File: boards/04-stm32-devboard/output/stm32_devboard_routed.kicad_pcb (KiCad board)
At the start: 2 copper layers, 60 x 40 mm, 17 parts, among them J1 SWD, U1 AMS1117-3.3, U2 STM32F103C8T6, Y1 8MHz

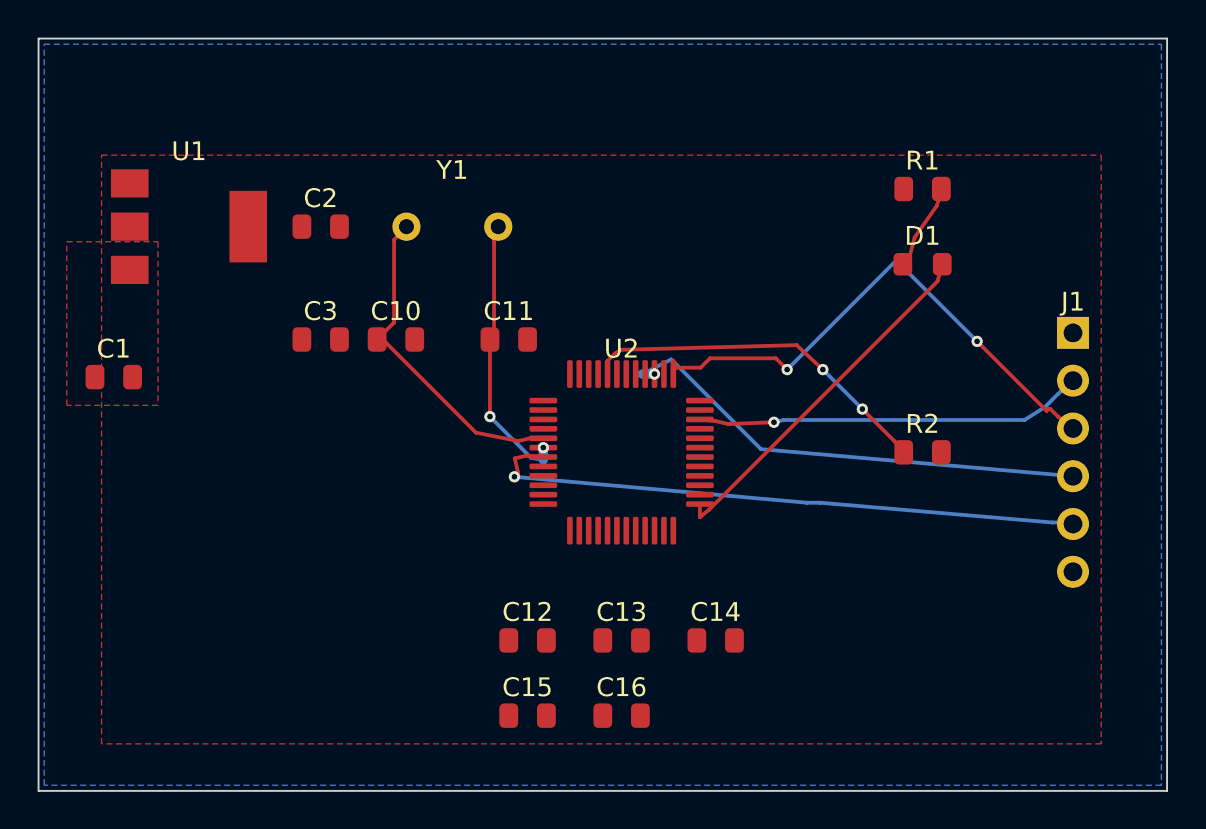
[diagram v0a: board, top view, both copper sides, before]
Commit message: feat(router,board-04): --micro-via stitch + --strict-in-pad-clearance opt-in (closes #3033) (#3038)
* feat(cli): expose --micro-via on outer kct stitch (forward from parser to subprocess)

The stitch_cmd module already supported --micro-via / --micro-via-size /
--micro-via-drill (PR #2786) but only at its own argparse layer.  The
outer ``kct stitch`` wrapper in cli/parser.py didn't register the
flags, so ``kct stitch board.kicad_pcb --net GND --micro-via`` returned
``error: unrecognized arguments: --micro-via``.

Fix: register the three micro-via args on ``stitch_parser`` (matching
the inner parser's dest names with the ``stitch_`` prefix) and forward
them through ``_run_stitch_command`` to the subprocess argv.  Behaviour
is unchanged when the flags are omitted; the inner defaults (0.3mm pad
/ 0.15mm drill) are forwarded as-is.

This unblocks board-04's LQFP-48 corner GND stitch (issue #3033): the
U2.23 corner pad now stitches cleanly with a micro-via after the
standard 0.6mm via collides with neighbour escape traces.  U2.8 is
still blocked (separate OSC_OUT-via track on B.Cu).

Co-Authored-By: Claude Opus 4.7 (1M context) <noreply@anthropic.com>

* fix(board-04): use --micro-via for GND stitch, refresh manufacturing bundle (closes #3033)

Adopts the new ``kct stitch --micro-via`` flag (added in the same PR's
feat(cli) commit) to recover board-04's U2.23 LQFP-48 corner GND pad
that the default 0.6mm via cannot fit between neighbour escape traces.
Stitcher reports go from 2 skipped GND pads -> 1 (U2.8 only, blocked
by an OSC_OUT B.Cu trace from the in-pad rescue -- separate cluster).

The regenerated manufacturing bundle restores manifest mtime > routed
PCB mtime so ``kct fleet status`` no longer reports the artifacts as
stale.

End-state on this PR vs. the pre-PR committed baseline:

| metric                          | pre-PR | post-PR | AC target |
|---------------------------------|--------|---------|-----------|
| nets complete / total           | 11/12  | 11/12 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
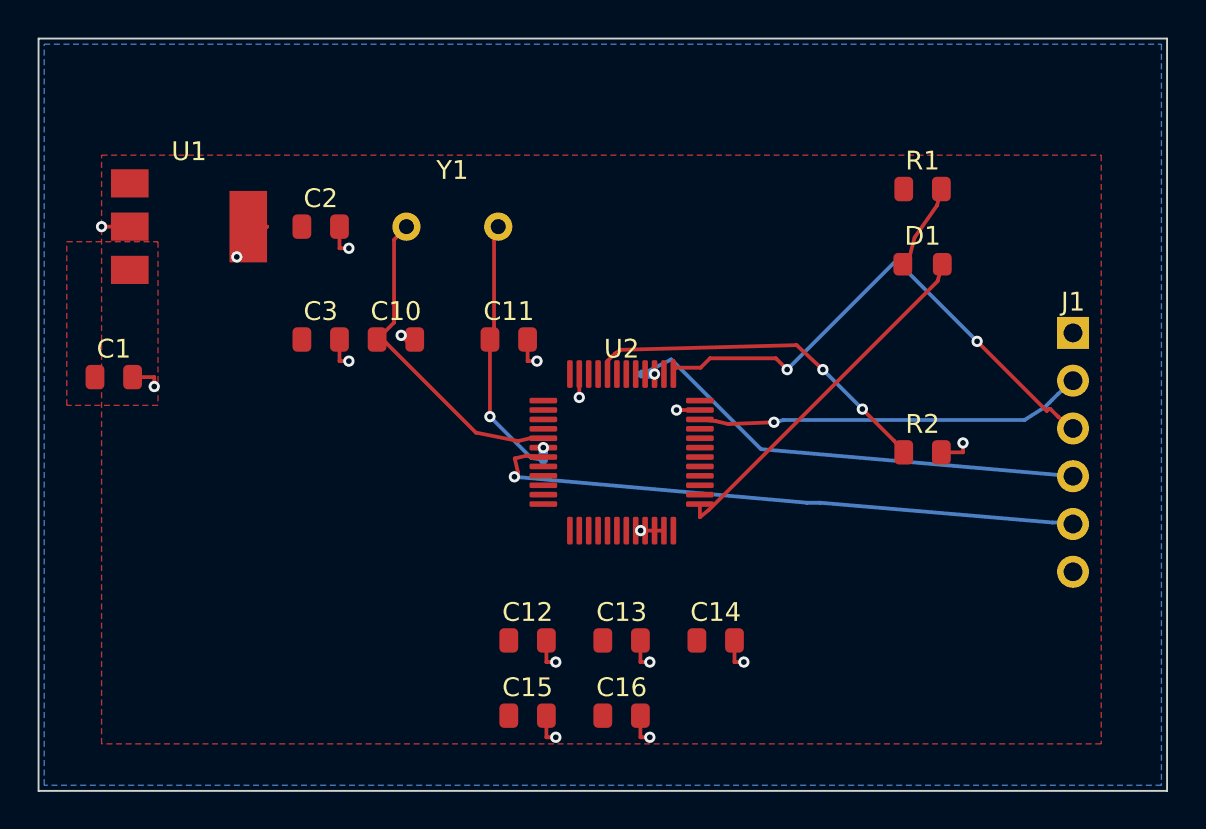
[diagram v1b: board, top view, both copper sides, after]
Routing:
- net GND: track 0.00 -> 26.5 mm, vias 0 -> 16

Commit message: feat(router): micro-via in-pad rescue for non-GND fine-pitch escape (closes #3118) (#3128)
When the standard manufacturer-floor via (0.6 mm OD / 0.3 mm drill on
jlcpcb-tier1) clips a foreign-net neighbour on a fine-pitch
QFP/SSOP/LQFP pad, the in-pad escape now retries with a micro-via
(default 0.3 mm OD / 0.15 mm drill) when the new
``--micro-via-in-pad-fallback`` flag is set.  The emitted via carries
``is_micro=True`` so it serialises as ``(via micro ...)`` and the
dimensions DRC exempts it from the standard min-via floors.

On board-04 (STM32 devboard, LQFP-48 0.5 mm-pitch), this resolves the
OSC_OUT cluster outright: pre-fix 4 errors (2 ``clearance_segment_via``
+ 2 ``clearance_pad_via`` at U2.5/U2.7) drop to 0.  The drc tolerance
floor for ``boards/04-stm32-devboard/output/stm32_devboard_routed.kicad_pcb``
is decremented 4 -> 1 (the remaining 1 is the historically-unstable
SWDIO/BOOT0 site at PCB (143.8, 119.7), separate cluster).

Implementation:
* ``EscapeRouter.__init__`` reads
  ``KICAD_TOOLS_MICRO_VIA_IN_PAD_FALLBACK`` /
  ``KICAD_TOOLS_MICRO_VIA_SIZE`` /
  ``KICAD_TOOLS_MICRO_VIA_DRILL`` env vars so the lazily-constructed
  router instances inherit the opt-in across all 3 construction sites
  (orchestrator + core) without new positional args.
* ``_try_in_pad_escape`` runs the micro-via retry inside the existing
  ``_via_clears_other_pads`` rejection branch (no new dispatcher args),
  re-checks geometry and clearance, and only commits the micro-via
  when both gates pass.
* CLI flags ``--micro-via-in-pad-fallback`` / ``--micro-via-size`` /
  ``--micro-via-drill`` added on both the outer ``kct route`` parser
  (forwarding) and the inner ``route_cmd.main`` (env-stamping).
* ``boards/04-stm32-devboard/generate_design.py`` now passes
  ``--micro-via-in-pad-fallback`` on its ``kct route`` invocation.

Micro-via preservation through the route pipeline (companion fixes to
#3124/#3126):
* ``EscapeRouter._apply_edge_clearance`` -- the edge-clamp rebuilt the
  Via w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
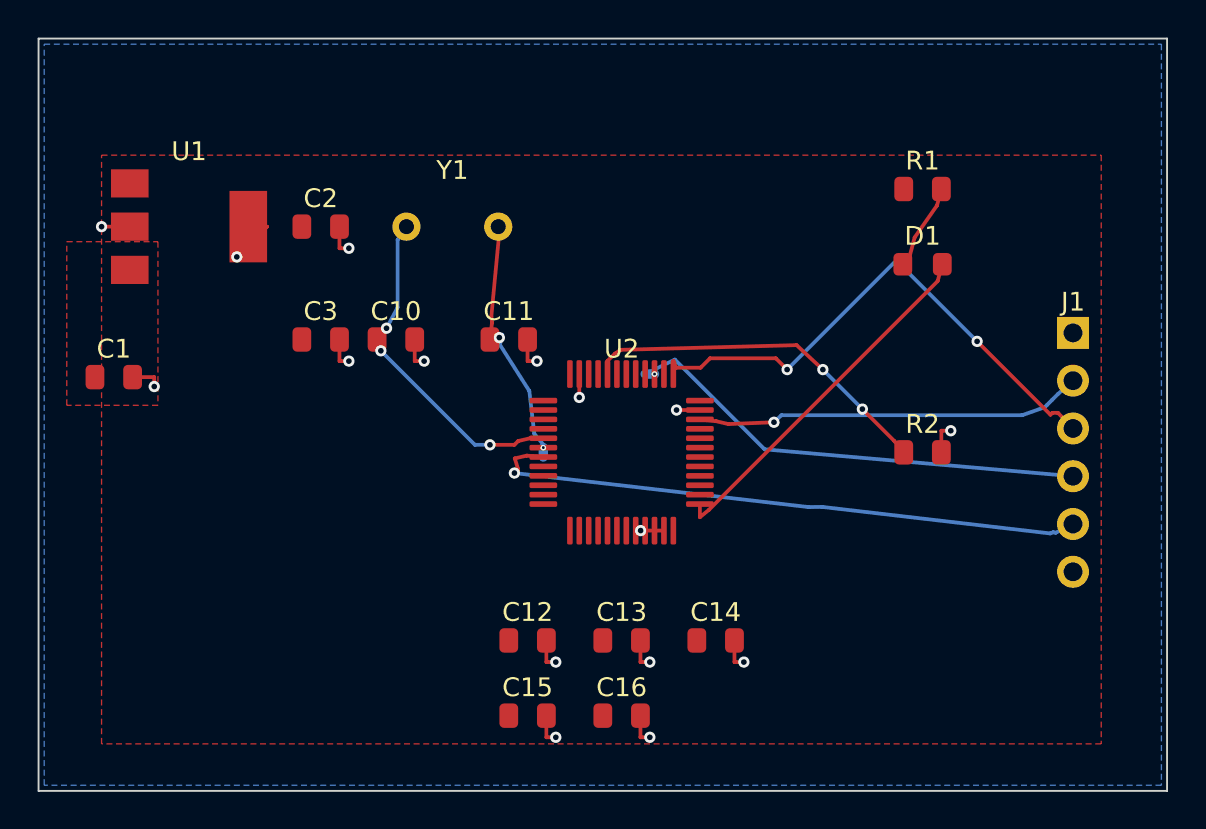
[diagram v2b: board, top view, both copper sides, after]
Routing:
- net OSC_IN: track 17.5 -> 17.9 mm, vias 0 -> 3

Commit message: fix(board-04): document NRST clearance regression, refresh routed PCB (closes #3266)
The post-#3128 clearance-tightening cluster (#3225/#3227 foreign-pad
clearance, #3232/#3248 Chebyshev -> Euclidean disc kernel, #3250
sub-cell pad-metal margin) correctly closes a ~0.125mm pad-clearance
corridor between U2.7 (NRST) and U2.8 (GND) that the prior committed
routed PCB exploited.  Re-running the production recipe now lands 8/9
signal nets routed (NRST stranded at J1.5).

Diagnosis:
- The prior committed PCB at PR #3128 had NRST F.Cu running through
  the U2.7/U2.8 channel at ~0.125mm pad clearance -- BELOW the
  jlcpcb-tier1 0.127mm minimum.  Verified by checking out 62918dfb and
  re-running the recipe: the recipe at that commit also produces 8/9,
  so the committed routed PCB at #3128 was hand-preserved from an
  earlier router state, not regenerated.
- The current router correctly refuses to thread NRST through the
  marginal corridor.  No single PR in the post-#3128 router cluster is
  the sole regression source; the cumulative tightening is correct
  behaviour.
- The refreshed PCB has 0 blocking DRC errors (vs 1
  clearance_segment_via on the prior committed artifact); 2 advisory
  connectivity findings (NRST + GND U2.8/U2.35 stitch skips) are
  excluded from the CI gate per DRCChecker.ADVISORY_RULE_IDS (#3074).

Functional implication: SWD hardware reset is unavailable
(software-mediated reset through the SWD probe is unaffected).
Recovery options documented in the tolerance YAML; underlying cluster
rides with #2834 manufacturing-ready.

Changes:
- Refresh boards/04-stm32-devboard/output/stm32_devboard_routed.kicad_pcb
  (and the input schematic/PCB which only diff by random UUIDs) via
  the production recipe.
- Drop the CI gate floor for board 04: 1 -> 0 (the refreshed PCB has
  no blocking errors; the prior 1-error SWDIO/BOOT0 clearance_segment_via
  is gone).
- Document the regression mechanism and recovery options in both
  generate_design.py::route_pcb and th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
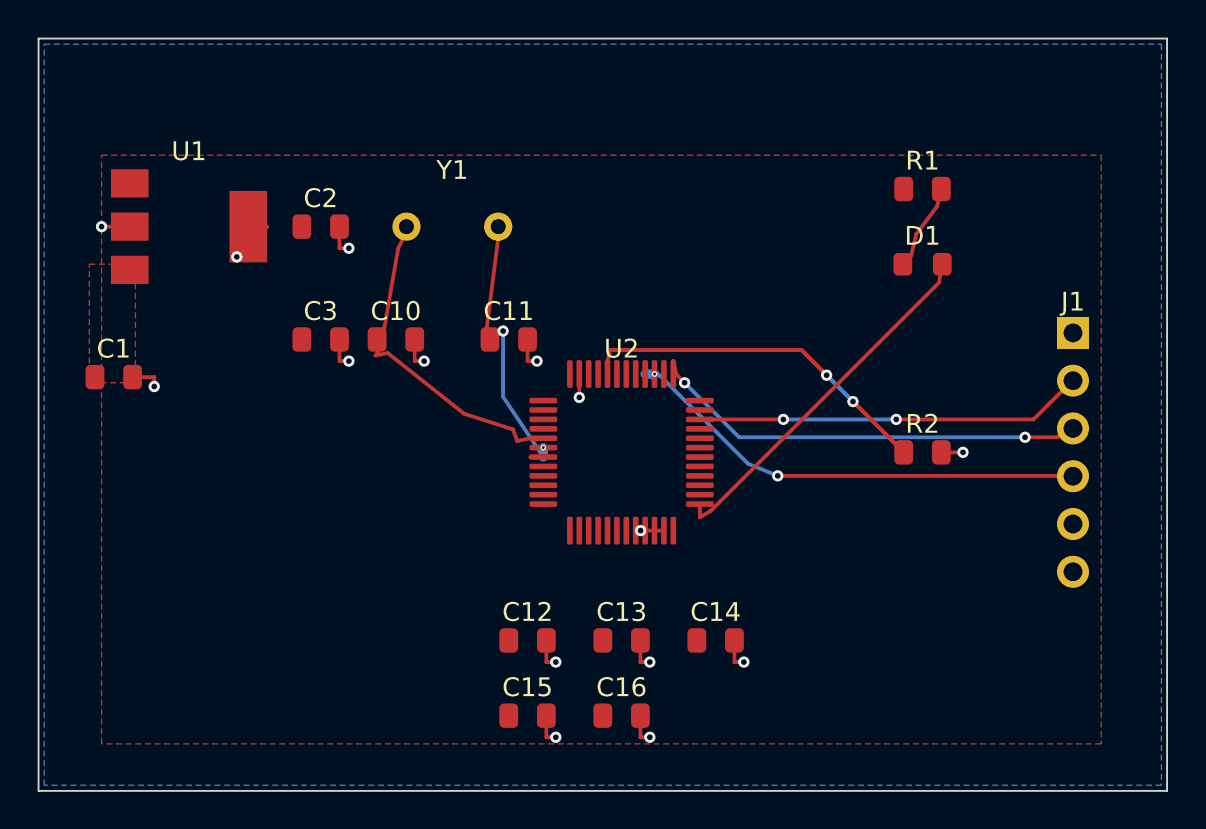
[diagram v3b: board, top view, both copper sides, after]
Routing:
- net NRST: track 32.4 -> 0.70 mm, vias 1 -> 0
- net SWCLK: track 28.8 -> 24.0 mm
- net GND: track 26.6 -> 24.9 mm, vias 16 -> 15
- net OSC_OUT: track 14.4 -> 15.0 mm
- net SWO: track 25.5 -> 25.3 mm, vias 1 -> 2
- net OSC_IN: track 17.9 -> 17.8 mm, vias 3 -> 0
- net SWDIO: track 20.6 -> 20.7 mm, vias 1 -> 2

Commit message: fix(router): seg-seg violations in negotiated quality tuple + demote-to-partial (refs #3411, closes #3433)
Closes #3433

Four coordinated fixes for the env-sensitive board-04 SWCLK/SWO
-0.200mm trace-overlap commits:

1. find_nets_with_segment_segment_violations completes the clearance
   matrix in the IterationMetrics lex tuple at all metric sites
   (core.py init/post/top-of-iter/final + two_phase.py equivalents),
   plus mid-iteration rip-up feed of both nets of each overlapping pair.
2. Demote-to-partial safety net: physically-overlapping copper
   (copper_overlap_only pairs) is stripped via greedy vertex cover
   rather than committed -- unrouted is advisory, overlap is a hard
   gate failure.
3. GridCollisionChecker.ignore_overflow scoped to genuinely overused
   cells (usage_count > 1): the #2303 blanket skip let the staircase
   compressor straighten SWO across SWCLK whenever ANY residual
   overflow existed (env-sensitive: rtree-equipped machines used the
   vector checker and never saw it).
4. Rect-aware stitch straight-trace pad check (find_all_pad_bboxes):
   the U2.8->U2.9 pad crossing was the lone remaining blocking error
   in the refreshed artifact.

Board-04 artifact refreshed at the production recipe: 9/9 routed
(NRST recovered per #3434), 0 blocking errors, floor stays 0.

Co-Authored-By: Claude Opus 4.7 <noreply@anthropic.com>
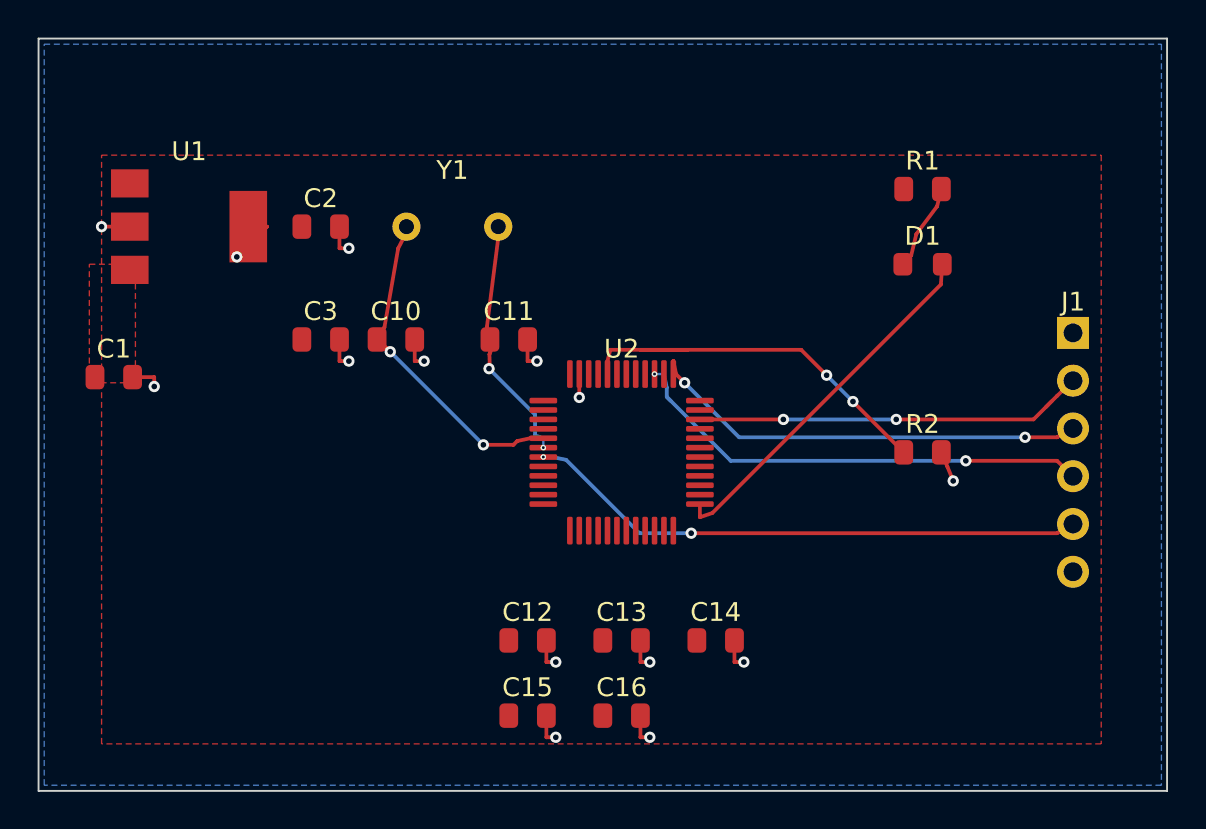
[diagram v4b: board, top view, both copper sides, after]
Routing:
- net NRST: track 0.70 -> 29.9 mm, vias 0 -> 2
- net OSC_OUT: track 15.0 -> 13.3 mm
- net GND: track 24.9 -> 24.2 mm, vias 15 -> 14
- net OSC_IN: track 17.8 -> 17.5 mm, vias 0 -> 2
